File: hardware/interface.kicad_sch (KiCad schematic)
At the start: 1 part

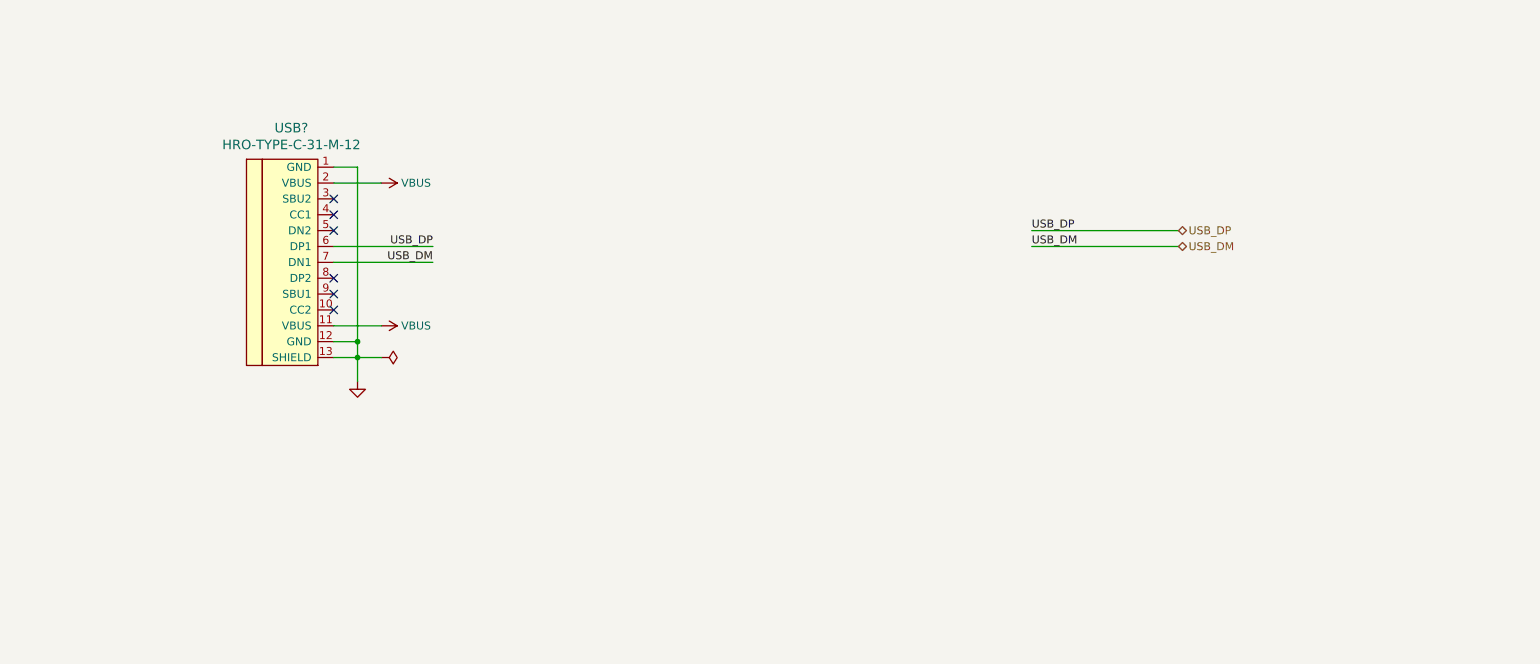
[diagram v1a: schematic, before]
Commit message: hw: Add DEBUG interface
- Add debug connector
- Adjust interface schematic
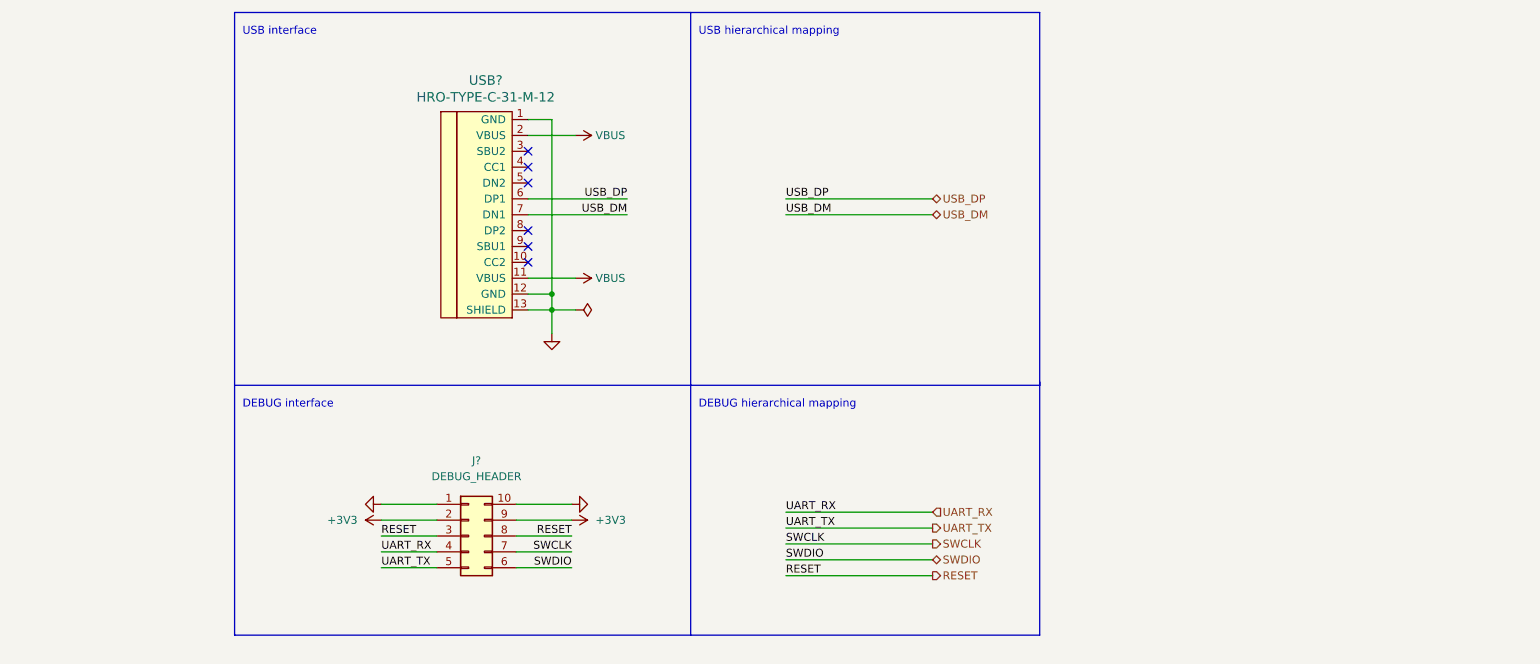
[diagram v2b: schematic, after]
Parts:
- added J?: DEBUG_HEADER, symbol Connector_Generic:Conn_02x05_Counter_Clockwise
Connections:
- net GND: now also J?.1 (Pin_1), J?.10 (Pin_10)
- new net +3V3: J?.2 (Pin_2), J?.9 (Pin_9)
- new net RESET: J?.3 (Pin_3), J?.8 (Pin_8)
- new net SWCLK: J?.7 (Pin_7)
- new net SWDIO: J?.6 (Pin_6)
- new net UART_RX: J?.4 (Pin_4)
- new net UART_TX: J?.5 (Pin_5)
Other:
- note added: "DEBUG hierarchical mapping"
- note added: "DEBUG interface"
- note added: "USB hierarchical mapping"
- note added: "USB interface"
- moved on the sheet: USB?

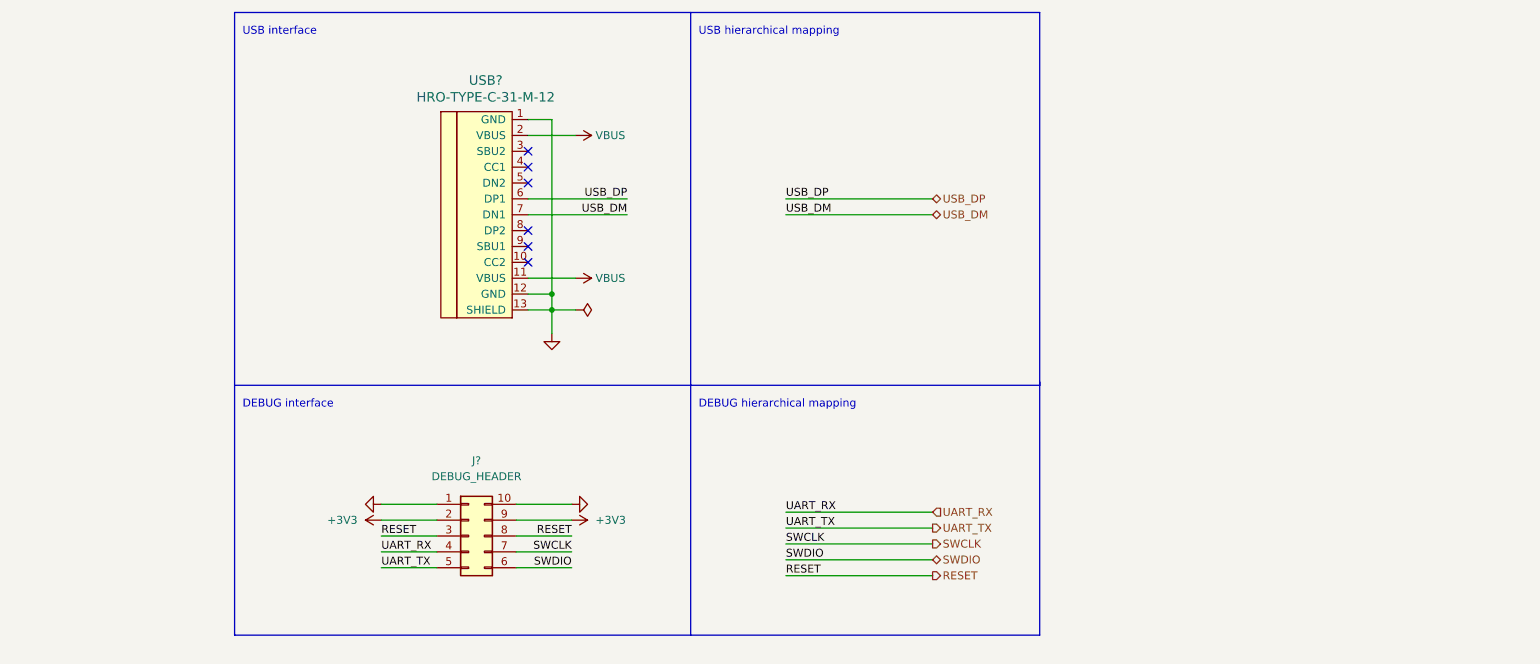
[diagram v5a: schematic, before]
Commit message: hw: Add LEDs and reset buton to interface
- Remove interface signal from CPU
- Add LEDS for ON, RX, TX, DIO signals
- Add button tor target reset
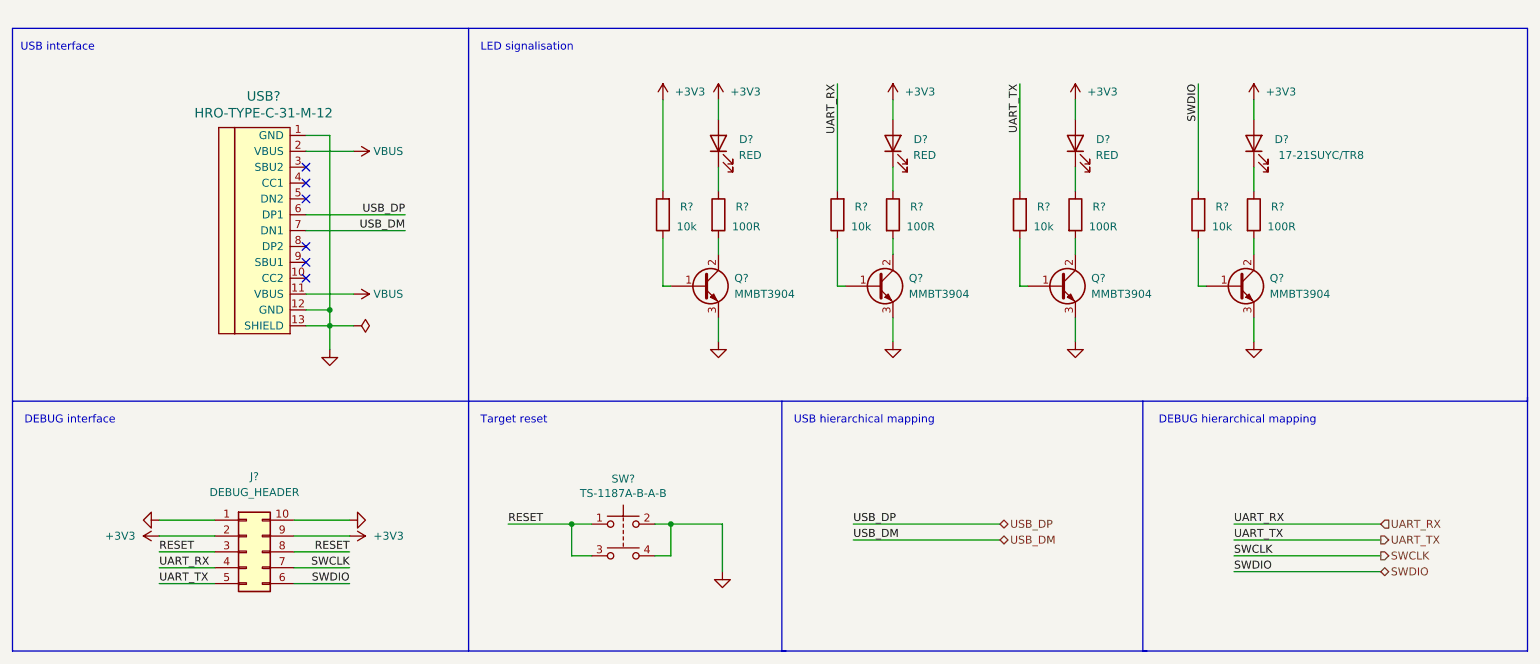
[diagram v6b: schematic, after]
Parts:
- added D? (x3): RED, LED_SMD:LED_0805_2012Metric_Pad1.15x1.40mm_HandSolder, symbol Device:LED
- added D?: 17-21SUYC/TR8, LED_SMD:LED_0805_2012Metric_Pad1.15x1.40mm_HandSolder, symbol Device:LED
- added Q? (x4): MMBT3904, Package_TO_SOT_SMD:SOT-23, symbol Device:Q_NPN_BCE
- added R? (x4): 10k, Resistor_SMD:R_0603_1608Metric_Pad0.98x0.95mm_HandSolder, symbol Device:R
- added R? (x4): 100R, Resistor_SMD:R_0603_1608Metric_Pad0.98x0.95mm_HandSolder, symbol Device:R
- added SW?: TS-1187A-B-A-B, TS-1187A-B-A-B:TS1187ABAB, symbol Switch:SW_Push_Dual
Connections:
- net +3V3: now also D?.2 (A), D?.2 (A), D?.2 (A), D?.2 (A), R?.2
- net GND: now also Q?.3 (E), Q?.3 (E), Q?.3 (E), Q?.3 (E), SW?.2, SW?.4
- net RESET: now also SW?.1, SW?.3
- net SWDIO: now also R?.2
- net UART_RX: now also R?.2
- net UART_TX: now also R?.2
- new net: Q?.1 (B), R?.1 (x4)
- new net: D?.1 (K), R?.1 (x4)
- new net: Q?.2 (C), R?.2 (x4)
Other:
- note added: "LED signalisation"
- note added: "Target reset"
- moved on the sheet: J?, USB?

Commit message: hw: Add the title block informations
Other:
- company: (none) -> Jan Krejčí
- title: (none) -> Pico probe
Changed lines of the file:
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@@
 (kicad_sch (version 20211123) (generator eeschema)
   (paper "A4")
+  (title_block
+    (title "Pico probe")
+    (date "2022-04-03")
+    (rev "22.04")
+    (company "Jan Krejčí")
+  )
   (junction (at 80.645 87.63) (diameter 0) (color 0 0 0 0)
   )
